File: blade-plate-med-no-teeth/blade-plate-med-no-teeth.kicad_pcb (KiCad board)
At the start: 2 copper layers, 37.1 x 45.1 mm, 3 parts

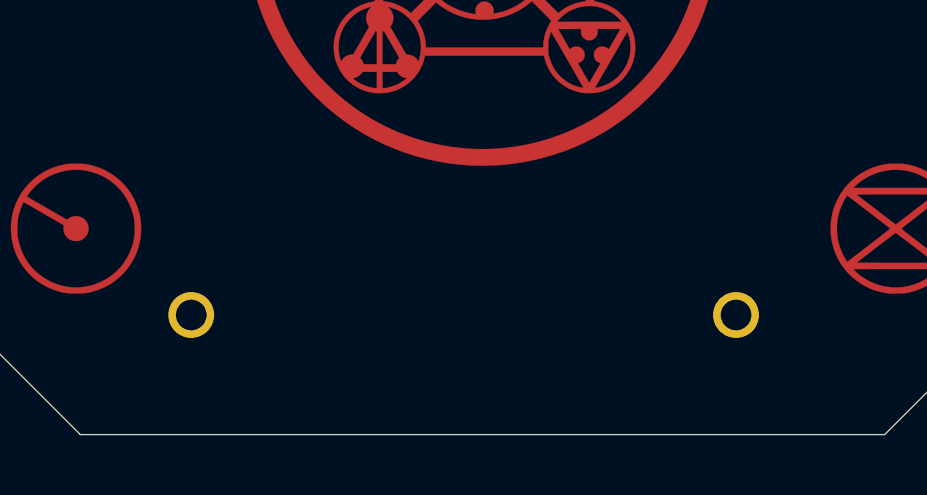
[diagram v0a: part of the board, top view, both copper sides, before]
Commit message: Added a little redundant metal on the guide bar between the batteries
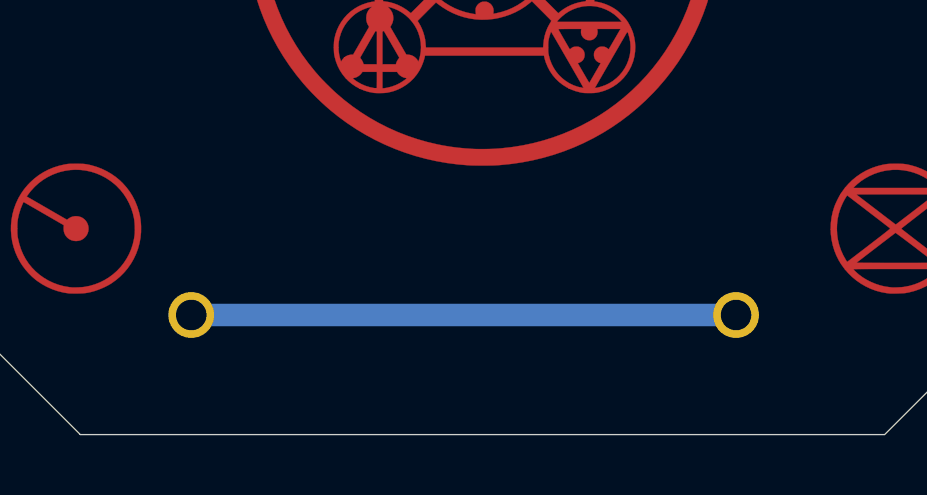
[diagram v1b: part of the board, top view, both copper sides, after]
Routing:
- net (no net): track 0.00 -> 18.2 mm
